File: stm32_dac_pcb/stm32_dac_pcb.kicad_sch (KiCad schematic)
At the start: 0 parts

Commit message: Add schematics for core bits
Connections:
- no-connect marks 0 -> 1
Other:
- added sheet dac_sheet (dac_sheet.kicad_sch)
- added sheet microcontroller_sheet (microcontroller_sheet.kicad_sch)
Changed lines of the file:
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@@
 (kicad_sch (version 20230121) (generator eeschema)
   (paper "USLetter")
+  (no_connect (at 107.95 64.77))
+  (wire (pts (xy 106.68 68.58) (xy 132.08 68.58))
+    (stroke (width 0) (type default))
+  )
+  (wire (pts (xy 106.68 53.34) (xy 132.08 53.34))
+    (stroke (width 0) (type default))
+  )
+  (wire (pts (xy 106.68 57.15) (xy 132.08 57.15))
+    (stroke (width 0) (type default))
+  )
+  (wire (pts (xy 106.68 49.53) (xy 132.08 49.53))
+    (stroke (width 0) (type default))
+  )
+  (wire (pts (xy 106.68 64.77) (xy 107.95 64.77))
+    (stroke (width 0) (type default))
+  )
+  (sheet (at 132.08 44.45) (size 45.72 27.94) (fields_autoplaced)
+    (stroke (width 0.1524) (type solid))
+    (fill (color 0 0 0 0.0000))
+    (property "Sheetname" "dac_sheet" (at 132.08 43.7384 0)
+      (effects (font (size 1.27 1.27)) (justify left bottom))
+    )
+    (property "Sheetfile" "dac_sheet.kicad_sch" (at 132.08 72.9746 0)
+      (effects (font (size 1.27 1.27)) (justify left top))
+    )
+    (pin "MUTE_CONTROL" input (at 132.08 68.58 180)
+      (effects (font (size 1.27 1.27)) (justify left))
+    )
+    (pin "LRCK" input (at 132.08 49.53 180)
+      (effects (font (size 1.27 1.27)) (justify left))
+    )
+    (pin "DIN" input (at 132.08 53.34 180)
+      (effects (font (size 1.27 1.27)) (justify left))
+    )
+    (pin "BCK" input (at 132.08 57.15 180)
+      (effects (font (size 1.27 1.27)) (justify left))
+    )
+    (instances
+      (project "stm32_dac_pcb"
+        (path "/c2a919d7-4260-41a9-9bc5-9737c1b4d769" (page "3"))
+      )
+    )
+  )
+  (sheet (at 71.12 44.45) (size 35.56 27.94) (fields_autoplaced)
+    (stroke (width 0.1524) (type solid))
+    (fill (color 0 0 0 0.0000))
+    (property "Sheetname" "microcontroller_sheet" (at 71.12 43.7384 0)
+      (effects (font (size 1.27 1.27)) (justify left bottom))
+    )
+    (property "Sheetfile" "microcontroller_sheet.kicad_sch" (at 71.12 72.9746 0)
+      (effects (font (size 1.27 1.27)) (justify left top))
+    )
+    (pin "I2S_MCK" output (at 106.68 64.77 0)
+      (effects (font (size 1.27 1.27)) (justify right))
+    )
+    (pin "MUTE_CONTROL" output (at 106.68 68.58 0)
+      (effects (font (size 1.27 1.27)) (justify right))
+    )
+    (pin "I2S_WS" output (at 106.68 49.53 0)
+      (effects (font (size 1.27 1.27)) (justify right))
+    )
+    (pin "I2S_SDI" output (at 106.68 53.34 0)
+      (effects (font (size 1.27 1.27)) (justify right))
+    )
+    (pin "I2S_BCK" output (at 106.68 57.15 0)
+      (effects (font (size 1.27 1.27)) (justify right))
+    )
+    (instances
+      (project "stm32_dac_pcb"
+        (path "/c2a919d7-4260-41a9-9bc5-9737c1b4d769" (page "2"))
+      )
+    )
+  )
   (sheet_instances
     (path "/" (page "1"))

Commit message: Layout and routing
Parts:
- added C205 (x4): 10u, Capacitor_SMD:C_1206_3216Metric_Pad1.33x1.80mm_HandSolder, symbol Device:C
- added JP101, JP102, JP103, JP104: SolderJumper_2_Open, Jumper:SolderJumper-2_P1.3mm_Open_RoundedPad1.0x1.5mm, symbol Jumper:SolderJumper_2_Open
- added U203 (x2): AP1117-33, Package_TO_SOT_SMD:SOT-223-3_TabPin2, symbol Regulator_Linear:AP1117-33
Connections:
- new net +3.3V: C205.1, JP102.2 (B), U203.2 (VO)
- new net +3.3VA: C205.1, JP102.1 (A), U203.2 (VO)
- new net +5V: C205.1, C205.1, U203.3 (VI), U203.3 (VI)
- new net GND: C205.2, C205.2, JP101.2 (B), U203.1 (GND)
- new net GNDA: C205.2, C205.2, JP101.1 (A), U203.1 (GND)
- new net dac_sheet/JACK_MIC: JP103.2 (B), JP104.2 (B)
- new net microcontroller_sheet/MIC_IN_1: JP103.1 (A)
- new net microcontroller_sheet/MIC_IN_2: JP104.1 (A)
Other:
- sheet dac_sheet ports: added JACK_MIC; removed none
- sheet microcontroller_sheet ports: added MIC_IN_1, MIC_IN_2; removed none
- note added: "3V3 Driver for Analog Systems (optional)"
- note added: "3V3 Driver for Digital Systems"
- note added: "Capacitor should be 10uF+ tantalum, with <0.5 ohms ESR."
- note added: "Must be bridged"
- note added: "Only bridge if analog regulator is not poplated"

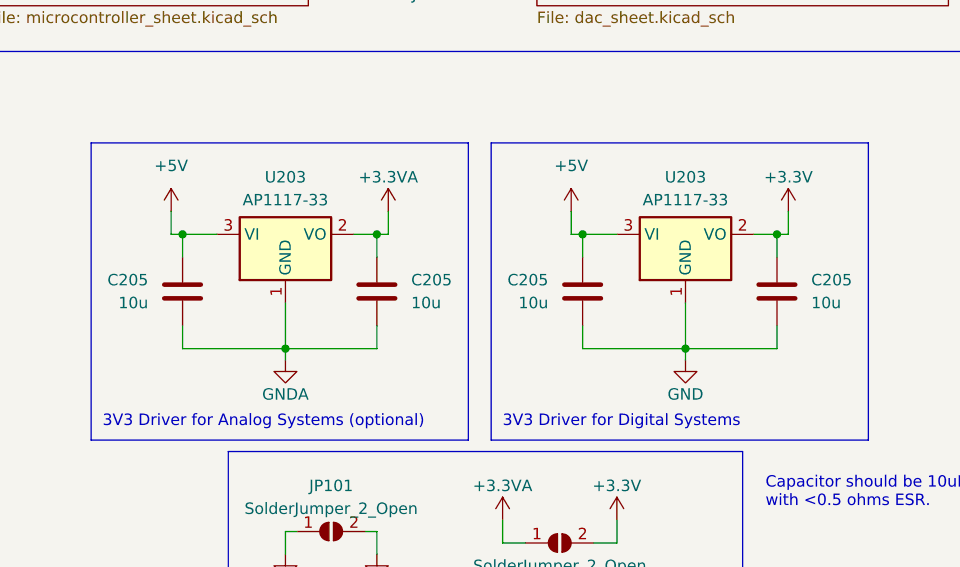
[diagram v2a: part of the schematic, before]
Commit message: Clean up tantalum capacitors
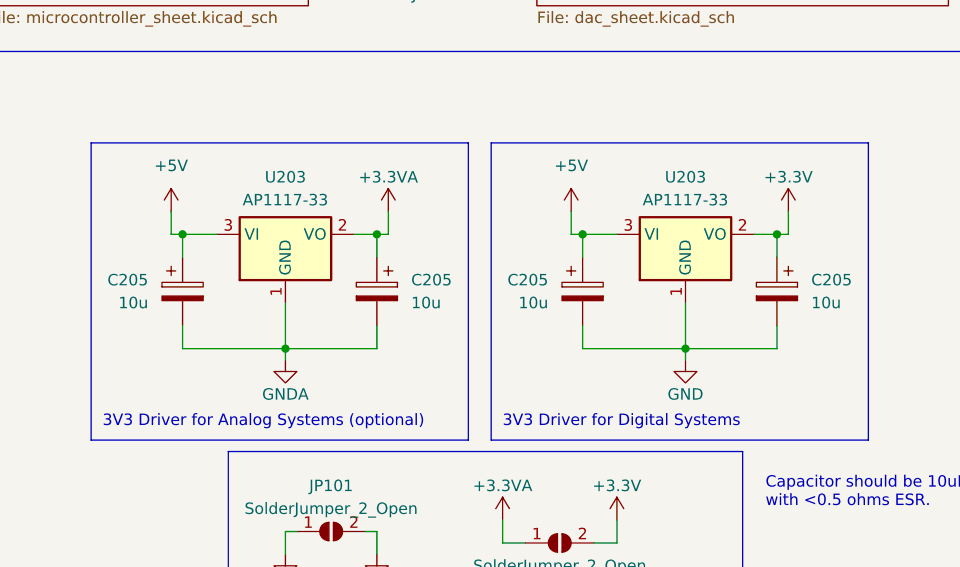
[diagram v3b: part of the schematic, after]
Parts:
- C205: footprint Capacitor_SMD:C_1206_3216Metric_Pad1.33x1.80mm_HandSolder -> 0_project_fp_lib:C_1206_3216Metric_Pad1.33x1.80mm_HandSolder_Polar; symbol Device:C -> Device:C_Polarized
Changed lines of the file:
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@@
     (effects (font (size 1.27 1.27)) (justify left bottom))
   )
-  (symbol (lib_id "Device:C") (at 52.07 132.08 0) (unit 1)
+  (symbol (lib_id "Device:C_Polarized") (at 52.07 132.08 0) (unit 1)
     (in_bom yes) (on_board yes) (dnp no)
     (property "Reference" "C205" (at 48.26 130.81 0)
@@
       (effects (font (size 1.27 1.27)) (justify right))
     )
-    (property "Footprint" "Capacitor_SMD:C_1206_3216Metric_Pad1.33x1.80mm_HandSolder" (at 53.0352 135.89 0)
+    (property "Footprint" "0_project_fp_lib:C_1206_3216Metric_Pad1.33x1.80mm_HandSolder_Polar" (at 53.0352 135.89 0)
       (effects (font (size 1.27 1.27)) hide)
     )
@@
     )
   )
-  (symbol (lib_id "Device:C") (at 96.52 132.08 0) (unit 1)
+  (symbol (lib_id "Device:C_Polarized") (at 96.52 132.08 0) (unit 1)
     (in_bom yes) (on_board yes) (dnp no)
     (property "Reference" "C205" (at 92.71 130.81 0)
@@
       (effects (font (size 1.27 1.27)) (justify right))
     )
-    (property "Footprint" "Capacitor_SMD:C_1206_3216Metric_Pad1.33x1.80mm_HandSolder" (at 97.4852 135.89 0)
+    (property "Footprint" "0_project_fp_lib:C_1206_3216Metric_Pad1.33x1.80mm_HandSolder_Polar" (at 97.4852 135.89 0)
       (effects (font (size 1.27 1.27)) hide)
     )
@@
     )
   )
-  (symbol (lib_id "Device:C") (at 73.66 132.08 0) (mirror y) (unit 1)
+  (symbol (lib_id "Device:C_Polarized") (at 73.66 132.08 0) (mirror y) (unit 1)
     (in_bom yes) (on_board yes) (dnp no)
     (property "Reference" "C205" (at 77.47 130.81 0)
@@
       (effects (font (size 1.27 1.27)) (justify right))
     )
-    (property "Footprint" "Capacitor_SMD:C_1206_3216Metric_Pad1.33x1.80mm_HandSolder" (at 72.6948 135.89 0)
+    (property "Footprint" "0_project_fp_lib:C_1206_3216Metric_Pad1.33x1.80mm_HandSolder_Polar" (at 72.6948 135.89 0)
       (effects (font (size 1.27 1.27)) hide)
     )
@@
     )
   )
-  (symbol (lib_id "Device:C") (at 118.11 132.08 0) (mirror y) (unit 1)
+  (symbol (lib_id "Device:C_Polarized") (at 118.11 132.08 0) (mirror y) (unit 1)
     (in_bom yes) (on_board yes) (dnp no)
     (property "Reference" "C205" (at 121.92 130.81 0)
@@
       (effects (font (size 1.27 1.27)) (justify right))
     )
-    (property "Footprint" "Capacitor_SMD:C_1206_3216Metric_Pad1.33x1.80mm_HandSolder" (at 117.1448 135.89 0)
-      (effects (font (size 1.27 1.27)) hide)
-    )
+    (property "Footprint" "0_project_fp_lib:C_1206_3216Metric_Pad1.33x1.80mm_HandSolder_Polar" (at 117.1448 135.89 0)
+      (effects (font (size 1.27 1.27)) hide)
+    )

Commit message: Mostly finish up
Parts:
- removed JP101: SolderJumper_2_Open, Jumper:SolderJumper-2_P1.3mm_Open_RoundedPad1.0x1.5mm, symbol Jumper:SolderJumper_2_Open
- added H101, H102: MountingHole, symbol Mechanical:MountingHole
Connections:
- net GNDA is gone; now on net GND: C205.2, C205.2, U203.1 (GND)
- no-connect marks 1 -> 0
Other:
- sheet microcontroller_sheet ports: added none; removed I2S_MCK
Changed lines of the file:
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@@
   (junction (at 96.52 125.73) (diameter 0) (color 0 0 0 0)
   )
-  (no_connect (at 67.31 85.09))
   (wire (pts (xy 118.11 125.73) (xy 115.57 125.73))
     (stroke (width 0) (type default))
@@
     (stroke (width 0) (type default))
   )
-  (wire (pts (xy 72.39 158.75) (xy 73.66 158.75))
-    (stroke (width 0) (type default))
-  )
   (wire (pts (xy 83.82 92.71) (xy 87.63 92.71))
     (stroke (width 0) (type default))
@@
     (stroke (width 0) (type default))
   )
+  (wire (pts (xy 63.5 158.75) (xy 73.66 158.75))
+    (stroke (width 0) (type default))
+  )
   (wire (pts (xy 73.66 125.73) (xy 73.66 128.27))
     (stroke (width 0) (type default))
   )
-  (wire (pts (xy 64.77 158.75) (xy 63.5 158.75))
-    (stroke (width 0) (type default))
-  )
   (wire (pts (xy 119.38 123.19) (xy 119.38 125.73))
     (stroke (width 0) (type default))
@@
   )
   (wire (pts (xy 96.52 135.89) (xy 96.52 138.43))
-    (stroke (width 0) (type default))
-  )
-  (wire (pts (xy 66.04 85.09) (xy 67.31 85.09))
     (stroke (width 0) (type default))
   )
@@
     )
   )
+  (symbol (lib_id "Mechanical:MountingHole") (at 19.05 189.23 0) (unit 1)
+    (in_bom yes) (on_board yes) (dnp no) (fields_autoplaced)
+    (property "Reference" "H102" (at 21.59 187.96 0)
+      (effects (font (size 1.27 1.27)) (justify left))
+    )
+    (property "Value" "MountingHole" (at 21.59 190.5 0)
+      (effects (font (size 1.27 1.27)) (justify left))
+    )
+    (property "Footprint" "" (at 19.05 189.23 0)
+      (effects (font (size 1.27 1.27)) hide)
+    )
+    (property "Datasheet" "~" (at 19.05 189.23 0)
+      (effects (font (size 1.27 1.27)) hide)
+    )
+    (instances
+      (project "stm32_dac_pcb"
+        (path "/c2a919d7-4260-41a9-9bc5-9737c1b4d769"
+          (reference "H102") (unit 1)
+        )
+      )
+    )
+  )
   (symbol (lib_id "Regulator_Linear:AP1117-33") (at 107.95 125.73 0) (unit 1)
     (in_bom yes) (on_board yes) (dnp no) (fields_autoplaced)
@@
     )
   )
-  (symbol (lib_id "Jumper:SolderJumper_2_Open") (at 68.58 158.75 0) (unit 1)
-    (in_bom yes) (on_board yes) (dnp no)
-    (property "Reference" "JP101" (at 68.58 153.67 0)
-      (effects (font (size 1.27 1.27)))
-    )
-    (property "Value" "SolderJumper_2_Open" (at 68.58 156.21 0)
-      (effects (font (size 1.27 1.27)))
-    )
-    (property "Footprint" "Jumper:SolderJumper-2_P1.3mm_Open_RoundedPad1.0x1.5mm" (at 68.58 158.75 0)
-      (effects (font (size 1.27 1.27)) hide)
-    )
-    (property "Datasheet" "~" (at 68.58 158.75 0)
-      (effects (font (size 1.27 1.27)) hide)
-    )
-    (pin "2")
-    (pin "1")
-    (instances
-      (project "stm32_dac_pcb"
-        (path "/c2a919d7-4260-41a9-9bc5-9737c1b4d769"
-          (reference "JP101") (unit 1)
-        )
-      )
-    )
-  )
   (symbol (lib_id "Regulator_Linear:AP1117-33") (at 63.5 125.73 0) (unit 1)
     (in_bom yes) (on_board yes) (dnp no) (fields_autoplaced)
@@
         (path "/c2a919d7-4260-41a9-9bc5-9737c1b4d769"
           (reference "C104") (unit 1)
+        )
+      )
+    )
+  )
+  (symbol (lib_id "Mechanical:MountingHole") (at 19.05 182.88 0) (unit 1)
+    (in_bom yes) (on_board yes) (dnp no) (fields_autoplaced)
+    (property "Reference" "H101" (at 21.59 181.61 0)
+      (effects (font (size 1.27 1.27)) (justify left))
+    )
+    (property "Value" "MountingHole" (at 21.59 184.15 0)
+      (effects (font (size 1.27 1.27)) (justify left))
+    )
+    (property "Footprint" "" (at 19.05 182.88 0)
+      (effects (font (size 1.27 1.27)) hide)
+    )
+    (property "Datasheet" "~" (at 19.05 182.88 0)
+      (effects (font (size 1.27 1.27)) hide)
+    )
+    (instances
+      (project "stm32_dac_pcb"
+        (path "/c2a919d7-4260-41a9-9bc5-9737c1b4d769"
+          (reference "H101") (unit 1)
         )
       )
@@
       (effects (font (size 1.27 1.27)) (justify left top))
     )
-    (pin "I2S_MCK" output (at 66.04 85.09 0)
-      (effects (font (size 1.27 1.27)) (justify right))
-    )
     (pin "MUTE_CONTROL" output (at 66.04 87.63 0)

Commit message: Small updates
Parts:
- H101, H102: footprint (none) -> MountingHole:MountingHole_2.2mm_M2
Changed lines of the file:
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@@
       (effects (font (size 1.27 1.27)) (justify left))
     )
-    (property "Footprint" "" (at 19.05 189.23 0)
+    (property "Footprint" "MountingHole:MountingHole_2.2mm_M2" (at 19.05 189.23 0)
       (effects (font (size 1.27 1.27)) hide)
     )
@@
       (effects (font (size 1.27 1.27)) (justify left))
     )
-    (property "Footprint" "" (at 19.05 182.88 0)
-      (effects (font (size 1.27 1.27)) hide)
-    )
+    (property "Footprint" "MountingHole:MountingHole_2.2mm_M2" (at 19.05 182.88 0)
+      (effects (font (size 1.27 1.27)) hide)
+    )
